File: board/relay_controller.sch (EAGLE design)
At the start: 51 parts, among them IC1 STM32F103C8T, IC3 AT24C, X1 RJ45-8L21-S, X2 RJ45-8L21-S

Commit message: add 3.3v output
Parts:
- C11: device eagle-ltspice:CC0402 -> eagle-ltspice:CC0603
- R59, R60, R61, R62: device rcl:R-EU_R0402 -> rcl:R-EU_R0603
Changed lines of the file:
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@@
 <grid distance="0.1" unitdist="inch" unit="inch" style="lines" multiple="1" display="no" altdistance="0.01" altunitdist="inch" altunit="inch"/>
 <layers>
-<layer number="1" name="Top" color="4" fill="1" visible="no" active="no"/>
-<layer number="2" name="Route2" color="1" fill="3" visible="no" active="no"/>
-<layer number="3" name="Route3" color="4" fill="3" visible="no" active="no"/>
-<layer number="4" name="Route4" color="1" fill="4" visible="no" active="no"/>
-<layer number="5" name="Route5" color="4" fill="4" visible="no" active="no"/>
-<layer number="6" name="Route6" color="1" fill="8" visible="no" active="no"/>
-<layer number="7" name="Route7" color="4" fill="8" visible="no" active="no"/>
-<layer number="8" name="Route8" color="1" fill="2" visible="no" active="no"/>
-<layer number="9" name="Route9" color="4" fill="2" visible="no" active="no"/>
-<layer number="10" name="Route10" color="1" fill="7" visible="no" active="no"/>
-<layer number="11" name="Route11" color="4" fill="7" visible="no" active="no"/>
-<layer number="12" name="Route12" color="1" fill="5" visible="no" active="no"/>
-<layer number="13" name="Route13" color="4" fill="5" visible="no" active="no"/>
-<layer number="14" name="Route14" color="1" fill="6" visible="no" active="no"/>
-<layer number="15" name="Route15" color="4" fill="6" visible="no" active="no"/>
-<layer number="16" name="Bottom" color="1" fill="1" visible="no" active="no"/>
-<layer number="17" name="Pads" color="2" fill="1" visible="no" active="no"/>
-<layer number="18" name="Vias" color="2" fill="1" visible="no" active="no"/>
-<layer number="19" name="Unrouted" color="6" fill="1" visible="no" active="no"/>
-<layer number="20" name="Dimension" color="15" fill="1" visible="no" active="no"/>
-<layer number="21" name="tPlace" color="7" fill="1" visible="no" active="no"/>
-<layer number="22" name="bPlace" color="7" fill="1" visible="no" active="no"/>
-<layer number="23" name="tOrigins" color="15" fill="1" visible="no" active="no"/>
-<layer number="24" name="bOrigins" color="15" fill="1" visible="no" active="no"/>
-<layer number="25" name="tNames" color="7" fill="1" visible="no" active="no"/>
-<layer number="26" name="bNames" color="7" fill="1" visible="no" active="no"/>
-<layer number="27" name="tValues" color="7" fill="1" visible="no" active="no"/>
-<layer number="28" name="bValues" color="7" fill="1" visible="no" active="no"/>
+<layer number="1" name="Top" color="4" fill="1" visible="yes" active="no"/>
+<layer number="2" name="Route2" color="1" fill="3" visible="yes" active="no"/>
+<layer number="3" name="Route3" color="4" fill="3" visible="yes" active="no"/>
+<layer number="4" name="Route4" color="1" fill="4" visible="yes" active="no"/>
+<layer number="5" name="Route5" color="4" fill="4" visible="yes" active="no"/>
+<layer number="6" name="Route6" color="1" fill="8" visible="yes" active="no"/>
+<layer number="7" name="Route7" color="4" fill="8" visible="yes" active="no"/>
+<layer number="8" name="Route8" color="1" fill="2" visible="yes" active="no"/>
+<layer number="9" name="Route9" color="4" fill="2" visible="yes" active="no"/>
+<layer number="10" name="Route10" color="1" fill="7" visible="yes" active="no"/>
+<layer number="11" name="Route11" color="4" fill="7" visible="yes" active="no"/>
+<layer number="12" name="Route12" color="1" fill="5" visible="yes" active="no"/>
+<layer number="13" name="Route13" color="4" fill="5" visible="yes" active="no"/>
+<layer number="14" name="Route14" color="1" fill="6" visible="yes" active="no"/>
+<layer number="15" name="Route15" color="4" fill="6" visible="yes" active="no"/>
+<layer number="16" name="Bottom" color="1" fill="1" visible="yes" active="no"/>
+<layer number="17" name="Pads" color="2" fill="1" visible="yes" active="no"/>
+<layer number="18" name="Vias" color="2" fill="1" visible="yes" active="no"/>
+<layer number="19" name="Unrouted" color="6" fill="1" visible="yes" active="no"/>
+<layer number="20" name="Dimension" color="15" fill="1" visible="yes" active="no"/>
+<layer number="21" name="tPlace" color="7" fill="1" visible="yes" active="no"/>
+<layer number="22" name="bPlace" color="7" fill="1" visible="yes" active="no"/>
+<layer number="23" name="tOrigins" color="15" fill="1" visible="yes" active="no"/>
+<layer number="24" name="bOrigins" color="15" fill="1" visible="yes" active="no"/>
+<layer number="25" name="tNames" color="7" fill="1" visible="yes" active="no"/>
+<layer number="26" name="bNames" color="7" fill="1" visible="yes" active="no"/>
+<layer number="27" name="tValues" color="7" fill="1" visible="yes" active="no"/>
+<layer number="28" name="bValues" color="7" fill="1" visible="yes" active="no"/>
 <layer number="29" name="tStop" color="7" fill="3" visible="no" active="no"/>
 <layer number="30" name="bStop" color="7" fill="6" visible="no" active="no"/>
@@
 <layer number="35" name="tGlue" color="7" fill="4" visible="no" active="no"/>
 <layer number="36" name="bGlue" color="7" fill="5" visible="no" active="no"/>
-<layer number="37" name="tTest" color="7" fill="1" visible="no" active="no"/>
-<layer number="38" name="bTest" color="7" fill="1" visible="no" active="no"/>
+<layer number="37" name="tTest" color="7" fill="1" visible="yes" active="no"/>
+<layer number="38" name="bTest" color="7" fill="1" visible="yes" active="no"/>
 <layer number="39" name="tKeepout" color="4" fill="11" visible="no" active="no"/>
 <layer number="40" name="bKeepout" color="1" fill="11" visible="no" active="no"/>
@@
 <layer number="44" name="Drills" color="7" fill="1" visible="no" active="no"/>
 <layer number="45" name="Holes" color="7" fill="1" visible="no" active="no"/>
-<layer number="46" name="Milling" color="3" fill="1" visible="no" active="no"/>
-<layer number="47" name="Measures" color="7" fill="1" visible="no" active="no"/>
-<layer number="48" name="Document" color="7" fill="1" visible="no" active="no"/>
-<layer number="49" name="Reference" color="7" fill="1" visible="no" active="no"/>
-<layer number="50" name="dxf" color="7" fill="1" visible="no" active="no"/>
-<layer number="51" name="tDocu" color="7" fill="1" visible="no" active="no"/>
-<layer number="52" name="bDocu" color="7" fill="1" visible="no" active="no"/>
-<layer number="53" name="tGND_GNDA" color="7" fill="9" visible="no" active="no"/>
-<layer number="54" name="bGND_GNDA" color="1" fill="9" visible="no" active="no"/>
-<layer number="56" name="wert" color="7" fill="1" visible="no" active="no"/>
-<layer number="57" name="tCAD" color="7" fill="1" visible="no" active="no"/>
-<layer number="59" name="tCarbon" color="7" fill="1" visible="no" active="no"/>
-<layer number="60" name="bCarbon" color="7" fill="1" visible="no" active="no"/>
+<layer number="46" name="Milling" color="3" fill="1" visible="yes" active="no"/>
+<layer number="47" name="Measures" color="7" fill="1" visible="yes" active="no"/>
+<layer number="48" name="Document" color="7" fill="1" visible="yes" active="no"/>
+<layer number="49" name="Reference" color="7" fill="1" visible="yes" active="no"/>
+<layer number="50" name="dxf" color="7" fill="1" visible="yes" active="no"/>
+<layer number="51" name="tDocu" color="7" fill="1" visible="yes" active="no"/>
+<layer number="52" name="bDocu" color="7" fill="1" visible="yes" active="no"/>
+<layer number="53" name="tGND_GNDA" color="7" fill="9" visible="yes" active="no"/>
+<layer number="54" name="bGND_GNDA" color="1" fill="9" visible="yes" active="no"/>
+<layer number="56" name="wert" color="7" fill="1" visible="yes" active="no"/>
+<layer number="57" name="tCAD" color="7" fill="1" visible="yes" active="no"/>
+<layer number="59" name="tCarbon" color="7" fill="1" visible="yes" active="no"/>
+<layer number="60" name="bCarbon" color="7" fill="1" visible="yes" active="no"/>
 <layer number="90" name="Modules" color="5" fill="1" visible="yes" active="yes"/>
 <layer number="91" name="Nets" color="2" fill="1" visible="yes" active="yes"/>
@@
 <part name="+3V30" library="supply1" deviceset="+3V3" device=""/>
 <part name="GND85" library="supply1" deviceset="GND" device=""/>
-<part name="R59" library="rcl" deviceset="R-EU_" device="R0402" value="10k"/>
+<part name="R59" library="rcl" deviceset="R-EU_" device="R0603" value="10k"/>
 <part name="GND86" library="supply1" deviceset="GND" device=""/>
-<part name="C11" library="eagle-ltspice" deviceset="C" device="C0402" value="10nF"/>
+<part name="C11" library="eagle-ltspice" deviceset="C" device="C0603" value="10nF"/>
 <part name="D18" library="diode" deviceset="BAS70-04" device=""/>
 <part name="+3V31" library="supply1" deviceset="+3V3" device=""/>
 <part name="GND87" library="supply1" deviceset="GND" device=""/>
-<part name="R60" library="rcl" deviceset="R-EU_" device="R0402" value="100"/>
-<part name="R61" library="rcl" deviceset="R-EU_" device="R0402" value="100"/>
-<part name="R62" library="rcl" deviceset="R-EU_" device="R0402" value="1k"/>
+<part name="R60" library="rcl" deviceset="R-EU_" device="R0603" value="100"/>
+<part name="R61" library="rcl" deviceset="R-EU_" device="R0603" value="100"/>
+<part name="R62" library="rcl" deviceset="R-EU_" device="R0603" value="1k"/>
 <part name="+3V11" library="supply1" deviceset="+3V3" device=""/>
 <part name="J1" library="SparkFun-Connectors" deviceset="CONN_03" device="SCREW"/>

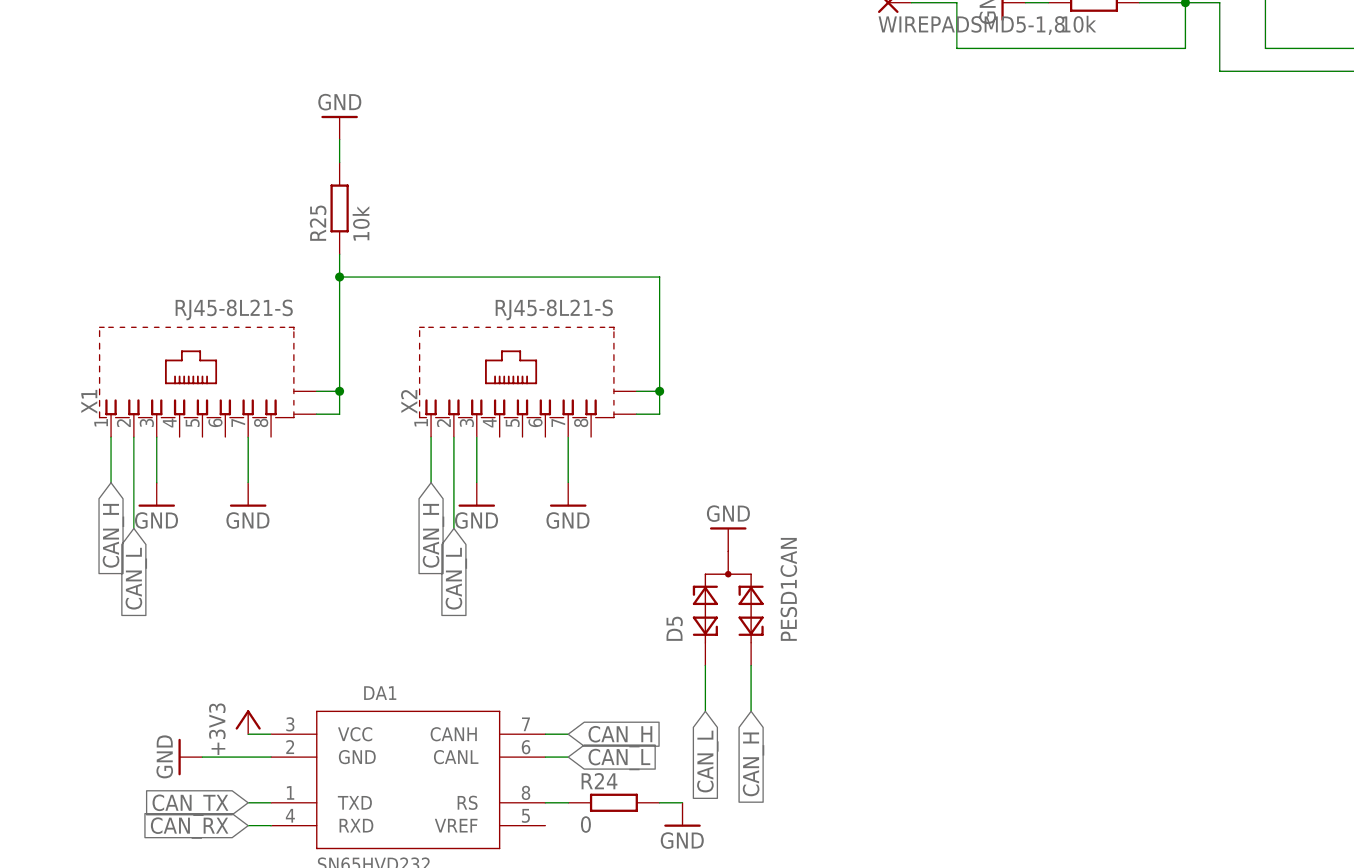
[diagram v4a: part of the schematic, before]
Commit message: power over can
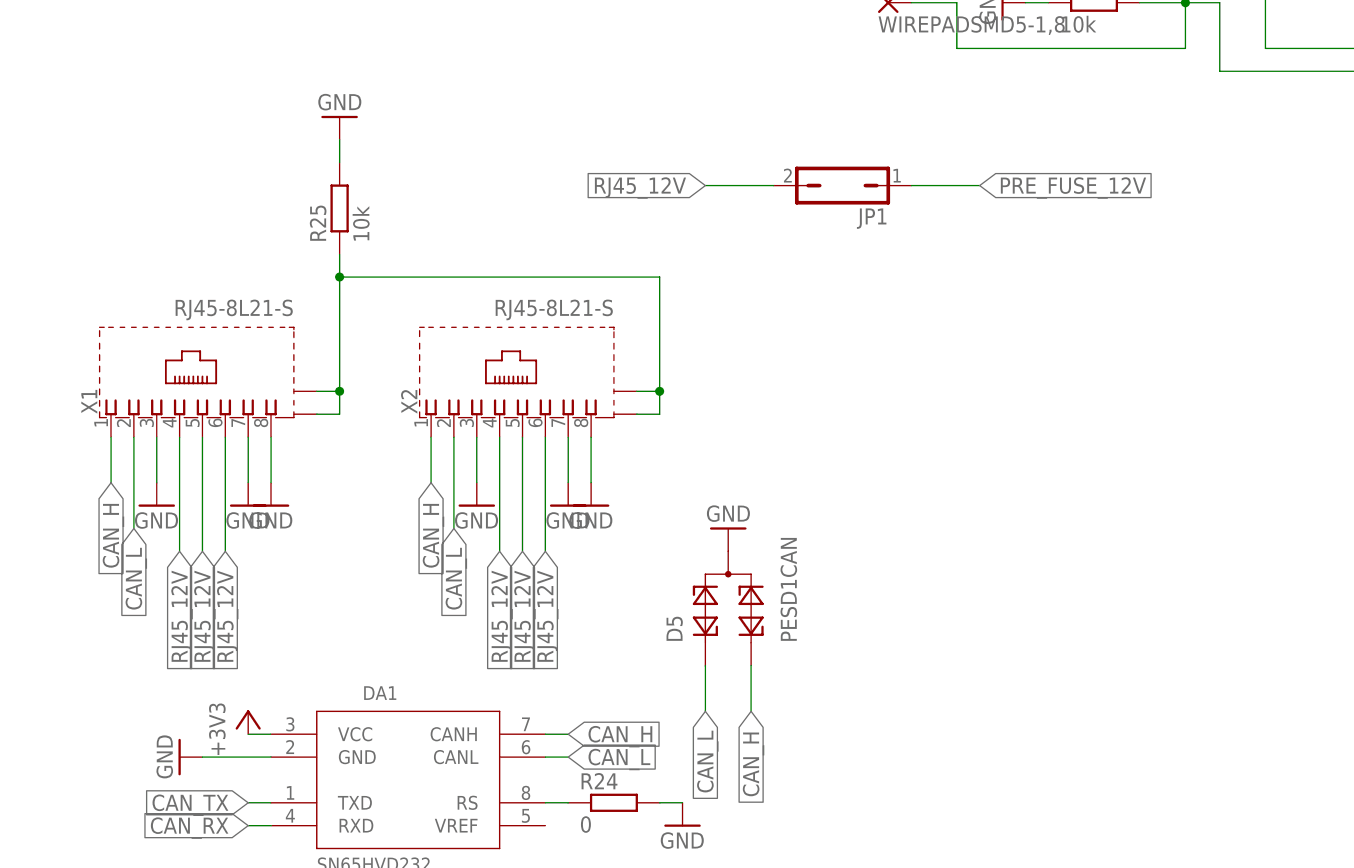
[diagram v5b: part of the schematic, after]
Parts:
- added JP1: (no value), jumper:JP1Q
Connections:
- removed net N$4: F2.2, J1.2
- new net PRE_FUSE_12V: F2.2, J1.2, JP1.1
- new net RJ45_12V: JP1.2, X1.4, X1.5, X1.6, X2.4, X2.5, X2.6
- net GND: now also X1.8, X2.8

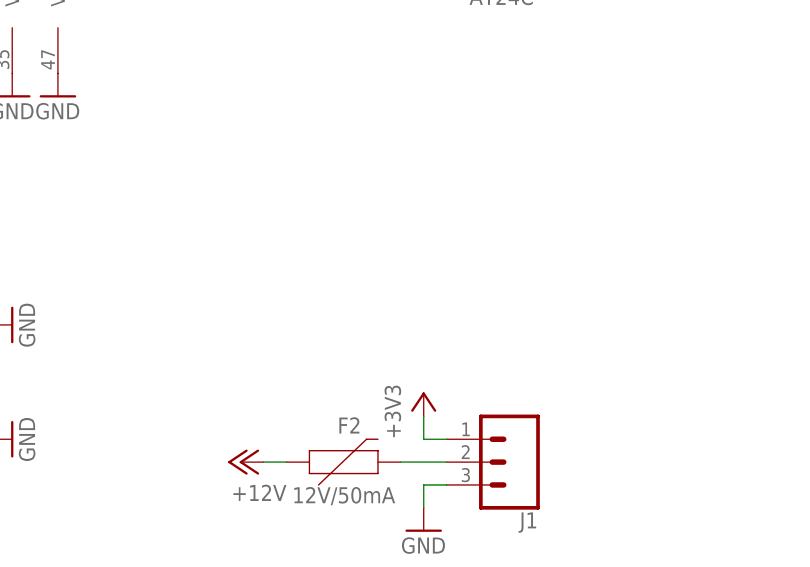
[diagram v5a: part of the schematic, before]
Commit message: add varistor
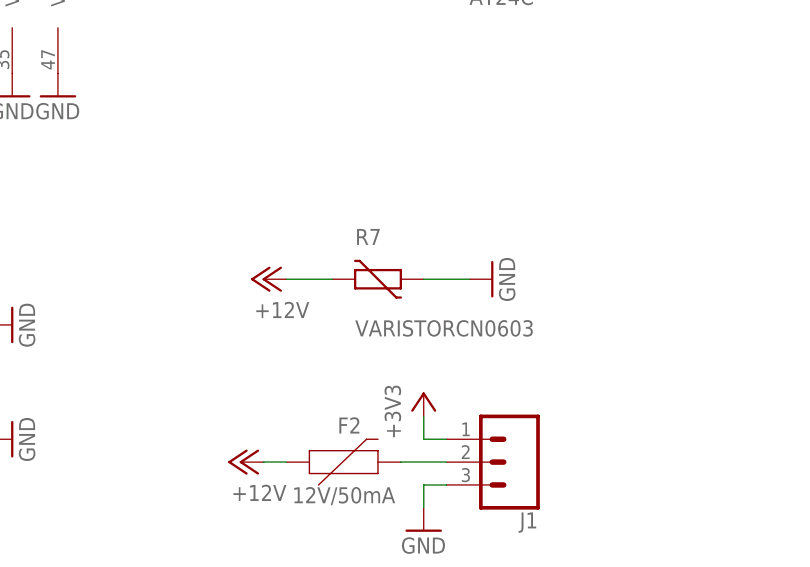
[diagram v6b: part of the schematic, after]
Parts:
- added R7: VARISTORCN0603, varistor:VARISTORCN0603
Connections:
- net +12V: now also R7.2
- net GND: now also R7.1
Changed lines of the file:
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@@
 <part name="GND9" library="supply1" deviceset="GND" device=""/>
 <part name="GND15" library="supply1" deviceset="GND" device=""/>
+<part name="R7" library="varistor" deviceset="VARISTOR" device="CN0603"/>
+<part name="P+3" library="supply1" deviceset="+12V" device=""/>
+<part name="GND16" library="supply1" deviceset="GND" device=""/>
 </parts>
 <sheets>
@@
 <instance part="GND9" gate="1" x="-149.86" y="-7.62"/>
 <instance part="GND15" gate="1" x="-185.42" y="-7.62"/>
+<instance part="R7" gate="G$1" x="88.9" y="45.72"/>
+<instance part="P+3" gate="1" x="76.2" y="45.72" rot="R90"/>
+<instance part="GND16" gate="1" x="101.6" y="45.72" rot="R90"/>
 </instances>
 <busses>
@@
 <pinref part="GND15" gate="1" pin="GND"/>
 </segment>
+<segment>
+<pinref part="R7" gate="G$1" pin="1"/>
+<pinref part="GND16" gate="1" pin="GND"/>
+<wire x1="99.06" y1="45.72" x2="93.98" y2="45.72" width="0.1524" layer="91"/>
+</segment>
 </net>
 <net name="+3V3" class="0">
@@
 <wire x1="76.2" y1="25.4" x2="78.74" y2="25.4" width="0.1524" layer="91"/>
 </segment>
+<segment>
+<pinref part="R7" gate="G$1" pin="2"/>
+<pinref part="P+3" gate="1" pin="+12V"/>
+<wire x1="78.74" y1="45.72" x2="83.82" y2="45.72" width="0.1524" layer="91"/>
+</segment>
 </net>

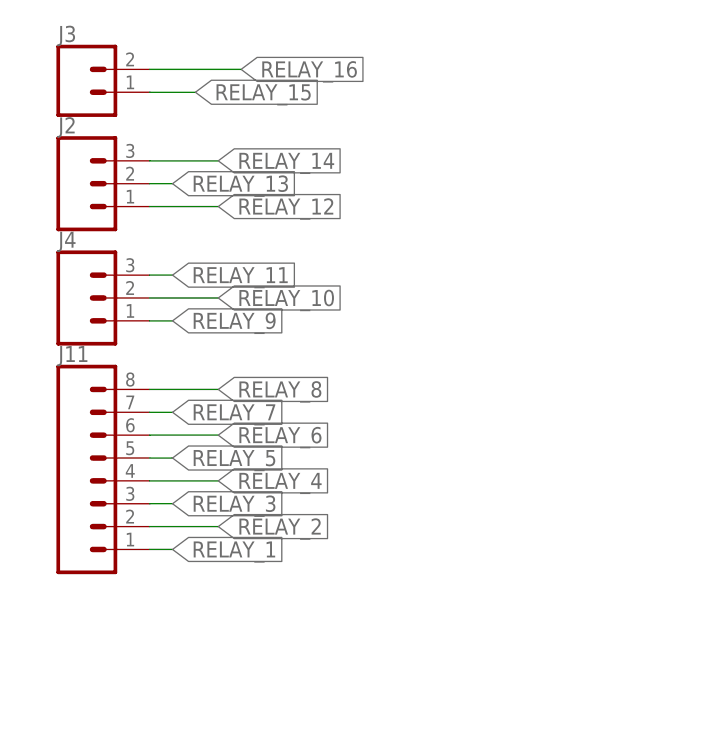
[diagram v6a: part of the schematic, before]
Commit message: add current limiting resistor
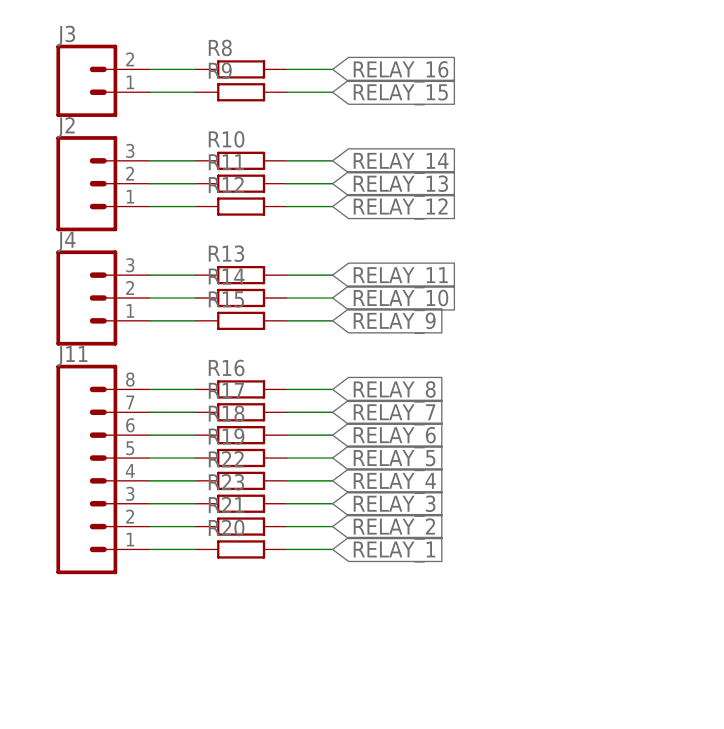
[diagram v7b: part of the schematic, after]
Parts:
- added R10, R11, R12, R13, R14, R15, R16, R17, R18, R19, R20, R21, R22, R23, R8, R9: (no value), resistor:R-EU_R0603
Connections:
- new net N$13: J2.3, R10.1
- new net N$14: J2.2, R11.1
- new net N$15: J2.1, R12.1
- new net N$16: J4.3, R13.1
- new net N$18: J4.2, R14.1
- new net N$19: J4.1, R15.1
- new net N$21: J11.8, R16.1
- new net N$22: J11.7, R17.1
- new net N$23: J11.6, R18.1
- new net N$24: J11.5, R19.1
- new net N$25: J11.1, R20.1
- new net N$26: J11.2, R21.1
- new net N$27: J11.4, R22.1
- new net N$28: J11.3, R23.1
- new net N$4: J3.2, R8.1
- new net N$9: J3.1, R9.1
- net RELAY_1: now also R20.2; no longer J11.1
- net RELAY_10: now also R14.2; no longer J4.2
- net RELAY_11: now also R13.2; no longer J4.3
- net RELAY_12: now also R12.2; no longer J2.1
- net RELAY_13: now also R11.2; no longer J2.2
- net RELAY_14: now also R10.2; no longer J2.3
- net RELAY_15: now also R9.2; no longer J3.1
- net RELAY_16: now also R8.2; no longer J3.2
- net RELAY_2: now also R21.2; no longer J11.2
- net RELAY_3: now also R23.2; no longer J11.3
- net RELAY_4: now also R22.2; no longer J11.4
- net RELAY_5: now also R19.2; no longer J11.5
- net RELAY_6: now also R18.2; no longer J11.6
- net RELAY_7: now also R17.2; no longer J11.7
- net RELAY_8: now also R16.2; no longer J11.8
- net RELAY_9: now also R15.2; no longer J4.1
